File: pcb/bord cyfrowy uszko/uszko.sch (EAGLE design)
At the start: 24 parts, among them U1 ADT7410TRZ

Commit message: pcb uszko
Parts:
- removed PTE6: (no value), wirepad:2,54/0,8
- added IC1: REG1117, burr-brown:REG1117
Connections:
- removed net N$60: PTE6.P, U$1.PTE6
- net +5V/1: now also IC1.VOUT
- net GND: now also IC1.GND
- net N$19: now also IC1.VIN
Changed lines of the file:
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@@
 </variantdefs>
 <classes>
-<class number="0" name="default" width="0" drill="0">
+<class number="0" name="default" width="0.6" drill="0.8">
 <clearance class="0" value="0.7"/>
 </class>
@@
 <part name="GND13" library="supply1" deviceset="GND" device=""/>
 <part name="SUPPLY10" library="supply2" deviceset="+5V/1" device="" value="3V3"/>
-<part name="PTE6" library="wirepad" deviceset="2,54/0,8" device=""/>
+<part name="IC1" library="burr-brown" deviceset="REG1117" device=""/>
+<part name="GND14" library="supply1" deviceset="GND" device=""/>
+<part name="SUPPLY11" library="supply2" deviceset="+5V/1" device="" value="3V3"/>
 </parts>
 <sheets>
@@
 <instance part="GND13" gate="1" x="-78.74" y="99.06" rot="R270"/>
 <instance part="SUPPLY10" gate="G$1" x="-78.74" y="111.76" rot="R90"/>
-<instance part="PTE6" gate="P" x="22.86" y="104.14"/>
+<instance part="IC1" gate="G$1" x="-160.02" y="114.3"/>
+<instance part="GND14" gate="1" x="-160.02" y="99.06"/>
+<instance part="SUPPLY11" gate="G$1" x="-144.78" y="114.3" rot="R270"/>
 </instances>
 <busses>
@@
 <segment>
 <wire x1="-50.8" y1="137.16" x2="-50.8" y2="86.36" width="0.1524" layer="92"/>
-<wire x1="-50.8" y1="86.36" x2="-50.8" y2="76.2" width="0.1524" layer="92"/>
-<wire x1="-50.8" y1="76.2" x2="-2.54" y2="76.2" width="0.1524" layer="92"/>
-<wire x1="-2.54" y1="76.2" x2="-2.54" y2="137.16" width="0.1524" layer="92"/>
+<wire x1="-50.8" y1="86.36" x2="-2.54" y2="86.36" width="0.1524" layer="92"/>
+<wire x1="-2.54" y1="86.36" x2="-2.54" y2="137.16" width="0.1524" layer="92"/>
 <wire x1="-2.54" y1="137.16" x2="-50.8" y2="137.16" width="0.1524" layer="92"/>
 <wire x1="-50.8" y1="137.16" x2="-50.8" y2="172.72" width="0.1524" layer="92"/>
@@
 <wire x1="-137.16" y1="129.54" x2="-172.72" y2="129.54" width="0.1524" layer="92"/>
 <wire x1="-172.72" y1="129.54" x2="-172.72" y2="177.8" width="0.1524" layer="92"/>
-<wire x1="-172.72" y1="177.8" x2="-55.88" y2="177.8" width="0.1524" layer="92"/>
-<wire x1="-55.88" y1="177.8" x2="-50.8" y2="172.72" width="0.1524" layer="92"/>
+<wire x1="-172.72" y1="177.8" x2="-50.8" y2="177.8" width="0.1524" layer="92"/>
 <wire x1="83.82" y1="137.16" x2="121.92" y2="137.16" width="0.1524" layer="92"/>
 <wire x1="121.92" y1="137.16" x2="121.92" y2="172.72" width="0.1524" layer="92"/>
 <wire x1="121.92" y1="172.72" x2="83.82" y2="172.72" width="0.1524" layer="92"/>
-<wire x1="-50.8" y1="172.72" x2="-50.8" y2="205.74" width="0.1524" layer="92"/>
+<wire x1="-50.8" y1="172.72" x2="-50.8" y2="177.8" width="0.1524" layer="92"/>
+<wire x1="-50.8" y1="177.8" x2="-50.8" y2="205.74" width="0.1524" layer="92"/>
 <wire x1="-50.8" y1="205.74" x2="-2.54" y2="205.74" width="0.1524" layer="92"/>
 <wire x1="-50.8" y1="86.36" x2="-137.16" y2="86.36" width="0.1524" layer="92"/>
@@
 <pinref part="GND13" gate="1" pin="GND"/>
 </segment>
+<segment>
+<pinref part="IC1" gate="G$1" pin="GND"/>
+<pinref part="GND14" gate="1" pin="GND"/>
+</segment>
 </net>
 <net name="+5V/1" class="0">
@@
 <pinref part="J1" gate="G$1" pin="6"/>
 <pinref part="SUPPLY10" gate="G$1" pin="+5V/1"/>
+</segment>
+<segment>
+<pinref part="IC1" gate="G$1" pin="VOUT"/>
+<pinref part="SUPPLY11" gate="G$1" pin="+5V/1"/>
 </segment>
 </net>
@@
 <junction x="-144.78" y="160.02"/>
 <pinref part="BAT+" gate="P" pin="P"/>
-<wire x1="-144.78" y1="172.72" x2="-160.02" y2="172.72" width="0.1524" layer="91"/>
+<wire x1="-144.78" y1="172.72" x2="-152.4" y2="172.72" width="0.1524" layer="91"/>
+<pinref part="IC1" gate="G$1" pin="VIN"/>
+<wire x1="-152.4" y1="172.72" x2="-160.02" y2="172.72" width="0.1524" layer="91"/>
+<wire x1="-172.72" y1="114.3" x2="-180.34" y2="114.3" width="0.1524" layer="91"/>
+<wire x1="-180.34" y1="114.3" x2="-180.34" y2="185.42" width="0.1524" layer="91"/>
+<wire x1="-180.34" y1="185.42" x2="-152.4" y2="185.42" width="0.1524" layer="91"/>
+<wire x1="-152.4" y1="185.42" x2="-152.4" y2="172.72" width="0.1524" layer="91"/>
+<junction x="-152.4" y="172.72"/>
 </segment>
 </net>
@@
 </segment>
 </net>
-<net name="N$60" class="0">
-<segment>
-<pinref part="U$1" gate="G$1" pin="PTE6"/>
-<pinref part="PTE6" gate="P" pin="P"/>
-</segment>
-</net>

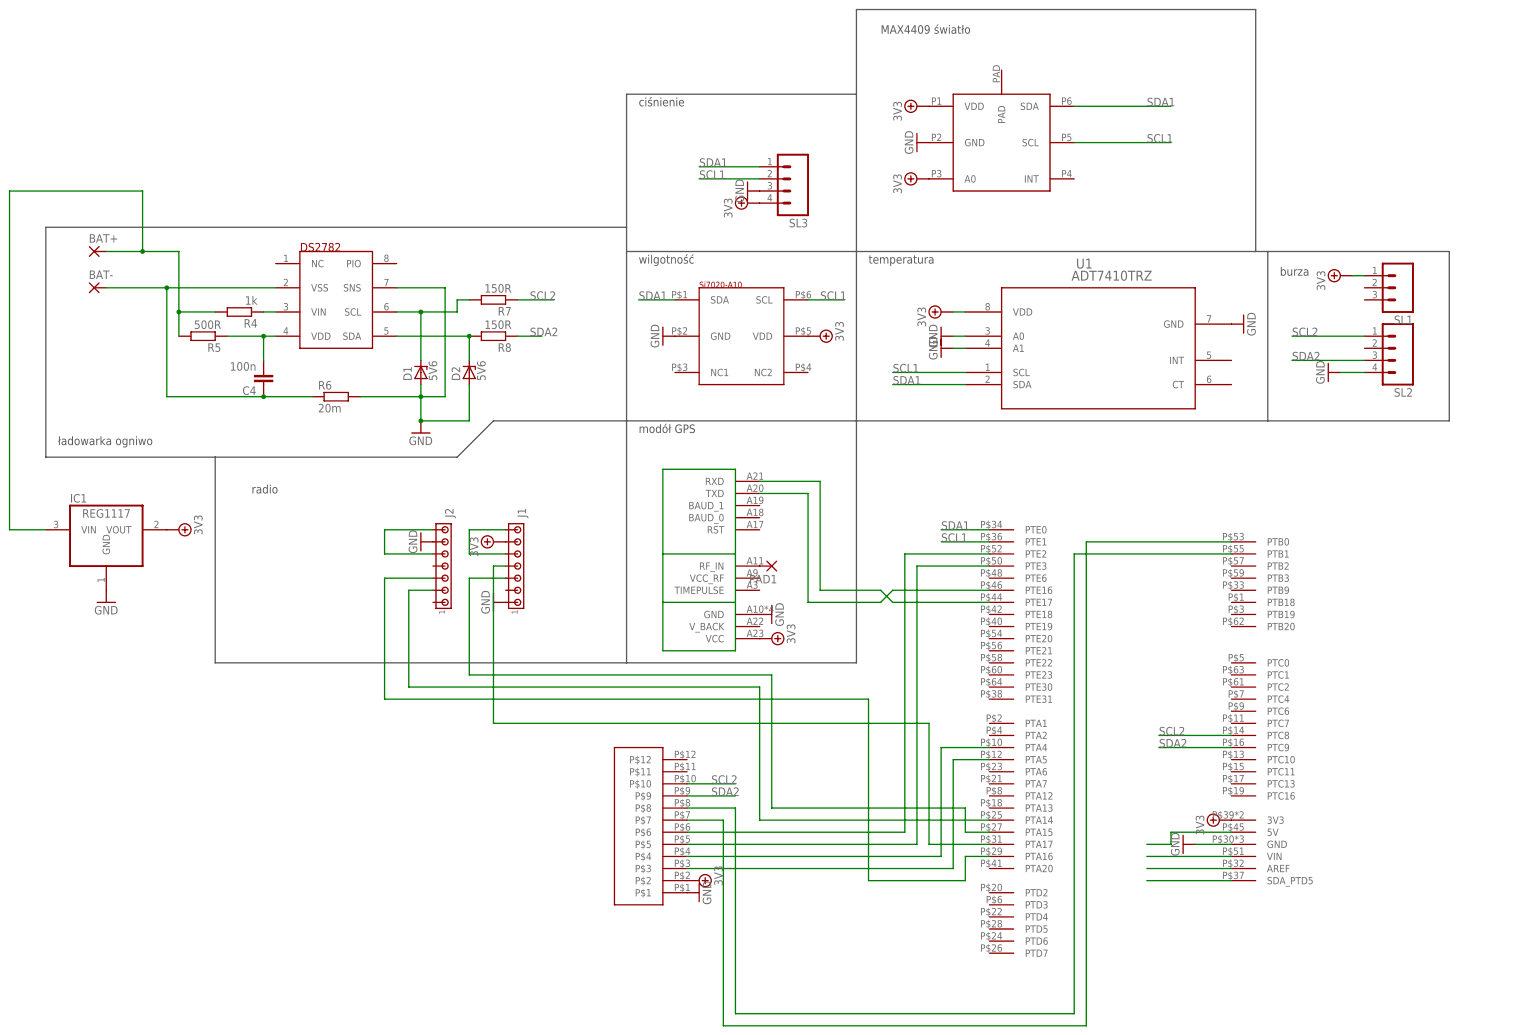
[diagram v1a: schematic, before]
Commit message: bord uszko, piout update
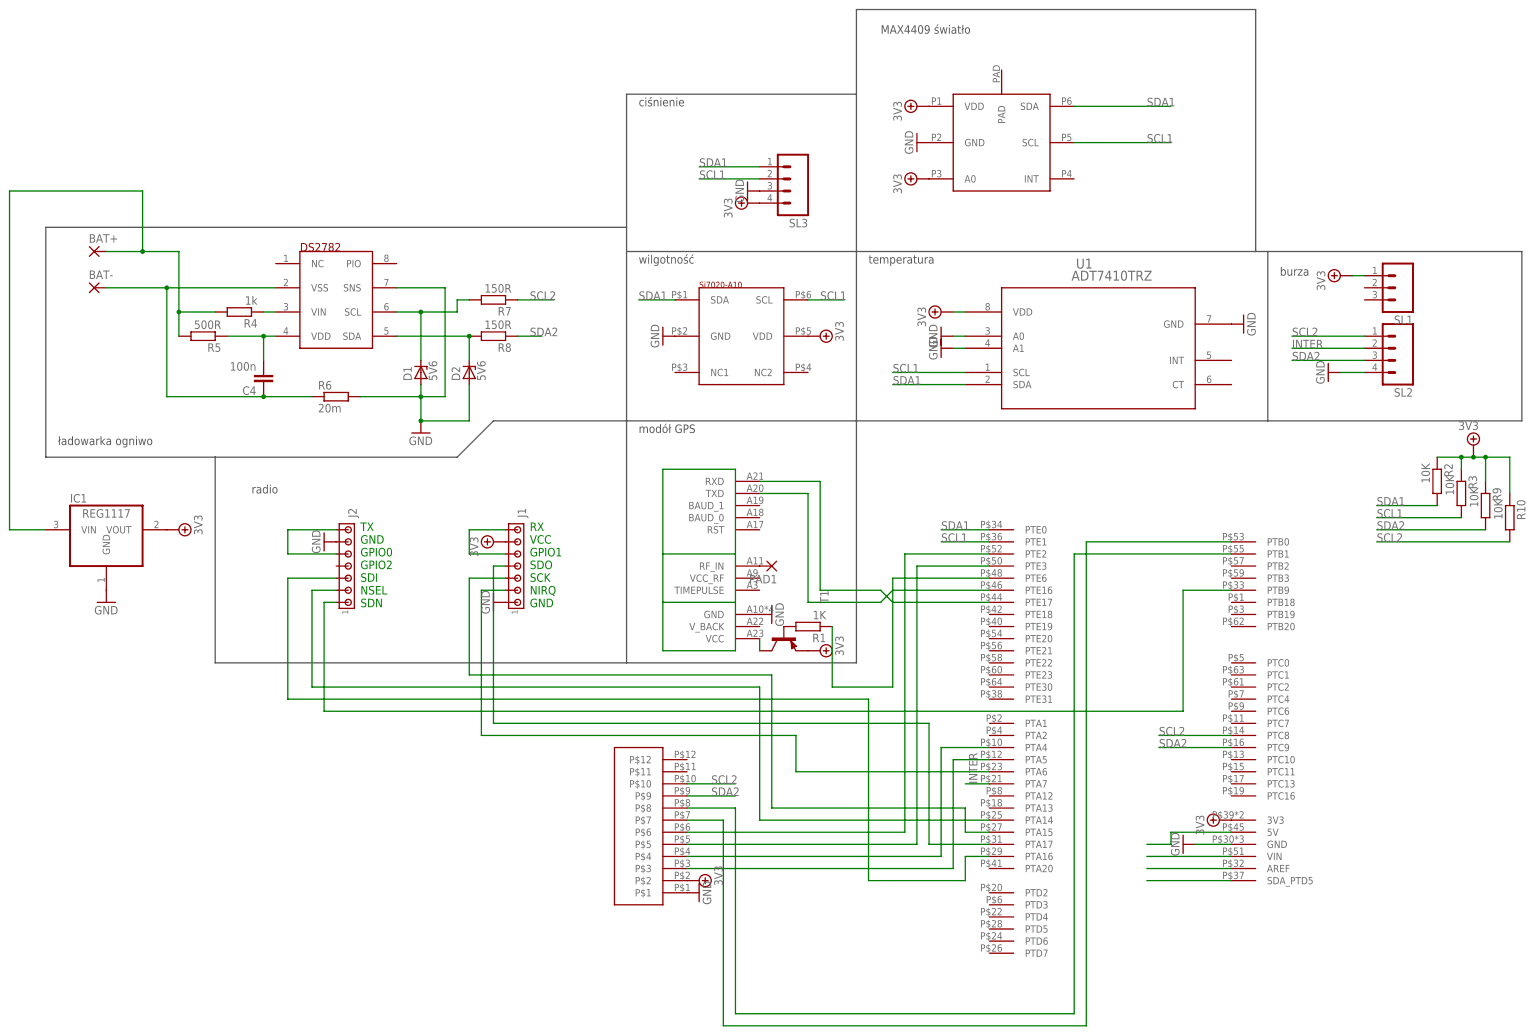
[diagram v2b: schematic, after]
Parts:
- added R1: 1K, resistor:R-EU_M0805
- added R10, R2, R3, R9: 10K, resistor:R-EU_M0805
- added T1: (no value), transistor:-PNP-SOT23-BCE
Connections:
- new net INTER: SL2.2, U$1.PTA7
- new net N$22: J1.2, U$1.PTA6
- new net N$23: T1.C, U$2.VCC
- new net N$24: R1.1, U$1.PTE6
- new net N$25: R1.2, T1.B
- new net N$26: J2.1, U$1.PTB9
- net +5V/1: now also R10.1, R2.1, R3.1, R9.1, T1.E; no longer U$2.VCC
- net SCL1: now also R3.2
- net SCL2: now also R10.2
- net SDA1: now also R2.2
- net SDA2: now also R9.2
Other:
- note added: "RX VCC GPIO1 SDO SCK NIRQ GND"
- note added: "TX GND GPIO0 GPIO2 SDI NSEL SDN"
- moved on the sheet: J2

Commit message: mgr, pcb uszko
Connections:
- removed net N$2: U$1.PTE16, U$2.TXD
- new net N$27: U$1.PTE17, U$2.TXD
- net N$1: now also U$1.PTE16; no longer U$1.PTE17
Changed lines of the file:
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@@
 </text>
 <text x="-48.26" y="203.2" size="1.778" layer="92">ciśnienie</text>
-<text x="-129.54" y="121.92" size="1.778" layer="92">radio</text>
+<text x="-132.08" y="124.46" size="1.778" layer="92">radio</text>
 <text x="-106.68" y="98.044" size="1.778" layer="91">TX
 GND
@@
 <pinref part="U$2" gate="G$1" pin="RXD"/>
 <wire x1="-10.16" y1="124.46" x2="-22.86" y2="124.46" width="0.1524" layer="91"/>
-<wire x1="-10.16" y1="101.6" x2="2.54" y2="101.6" width="0.1524" layer="91"/>
-<wire x1="2.54" y1="101.6" x2="5.08" y2="99.06" width="0.1524" layer="91"/>
-<pinref part="U$1" gate="G$1" pin="PTE17"/>
-<wire x1="5.08" y1="99.06" x2="25.4" y2="99.06" width="0.1524" layer="91"/>
-</segment>
-</net>
-<net name="N$2" class="0">
-<segment>
-<wire x1="-12.7" y1="99.06" x2="-12.7" y2="121.92" width="0.1524" layer="91"/>
-<pinref part="U$2" gate="G$1" pin="TXD"/>
-<wire x1="-12.7" y1="121.92" x2="-22.86" y2="121.92" width="0.1524" layer="91"/>
+<wire x1="-10.16" y1="101.6" x2="25.4" y2="101.6" width="0.1524" layer="91"/>
 <pinref part="U$1" gate="G$1" pin="PTE16"/>
-<wire x1="25.4" y1="101.6" x2="5.08" y2="101.6" width="0.1524" layer="91"/>
-<wire x1="5.08" y1="101.6" x2="2.54" y2="99.06" width="0.1524" layer="91"/>
-<wire x1="2.54" y1="99.06" x2="-12.7" y2="99.06" width="0.1524" layer="91"/>
 </segment>
 </net>
@@
 </segment>
 </net>
+<net name="N$27" class="0">
+<segment>
+<pinref part="U$1" gate="G$1" pin="PTE17"/>
+<wire x1="-12.7" y1="99.06" x2="-12.7" y2="121.92" width="0.1524" layer="91"/>
+<pinref part="U$2" gate="G$1" pin="TXD"/>
+<wire x1="-12.7" y1="121.92" x2="-22.86" y2="121.92" width="0.1524" layer="91"/>
+<wire x1="25.4" y1="99.06" x2="-12.7" y2="99.06" width="0.1524" layer="91"/>
+</segment>
+</net>

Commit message: + ADC
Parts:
- removed J1, J2: (no value), con-amp:MTA07-100
- added R11, R12, R13: 1K, resistor:R-EU_M0805
- added U$3: 2X7PIN, ref-packages:2X7PIN
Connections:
- new net N$28: R12.2, U$2.BAUD_0
- new net N$29: R11.2, U$2.BAUD_1
- new net N$30: R13.2, U$2.RST
- net +5V/1: now also U$3.P$9; no longer J1.6
- net GND: now also R11.1, U$3.P$14, U$3.P$2; no longer J1.1, J2.6
- net N$15: now also U$3.P$1, U$3.P$3; no longer J2.5, J2.7
- net N$16: now also U$3.P$10, U$3.P$8; no longer J1.5, J1.7
- net N$17: now also U$3.P$6; no longer J2.2
- net N$18: now also U$3.P$12; no longer J1.3
- net N$20: now also U$3.P$5; no longer J2.3
- net N$21: now also U$3.P$11; no longer J1.4
- net N$22: now also U$3.P$13; no longer J1.2
- net N$23: now also R12.1, R13.1
- net N$26: now also U$3.P$7; no longer J2.1
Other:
- moved on the sheet: R1, T1
